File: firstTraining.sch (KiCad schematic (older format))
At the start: 11 parts, among them T1 Transformer_1P_SS, U1 L7805, U2 L78L33_SO8

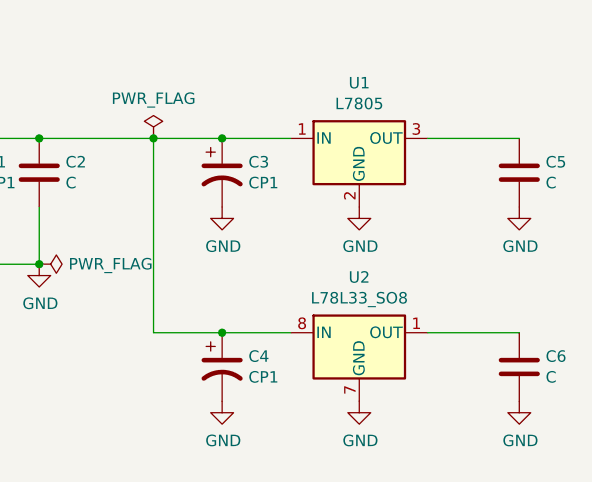
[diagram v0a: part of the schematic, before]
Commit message: GND配線の番号付与追加, 配置実施
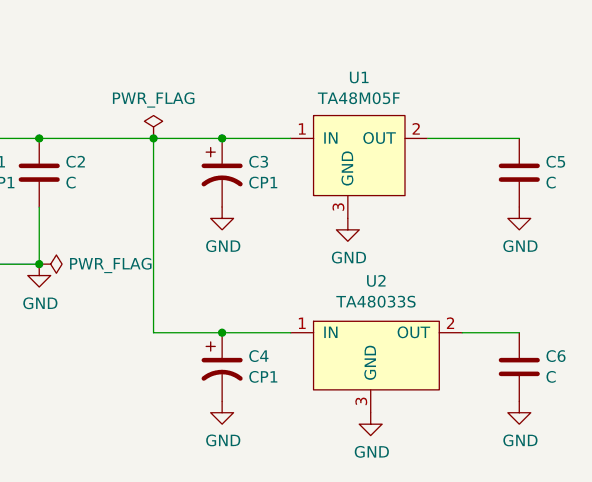
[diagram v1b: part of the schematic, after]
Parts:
- removed U1: L7805, Connector:FanPinHeader_1x03_P2.54mm_Vertical, symbol Regulator_Linear:L7805
- removed U2: L78L33_SO8, Connector:FanPinHeader_1x03_P2.54mm_Vertical, symbol Regulator_Linear:L78L33_SO8
- added U1: TA48M05F, Connector_PinHeader_2.54mm:PinHeader_1x03_P2.54mm_Vertical, symbol newLib:TA48M05F
- added U2: TA48033S, Connector_PinHeader_2.54mm:PinHeader_1x03_P2.54mm_Vertical, symbol newLib:TA48033S
- C2: footprint Capacitor_THT:CP_Radial_D10.0mm_P5.00mm -> Capacitor_THT:C_Disc_D3.0mm_W1.6mm_P2.50mm
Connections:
- net GND: now also U1.3 (GND), U2.3 (GND)
- net at C1.1, C2.1, C3.1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: now also U1.1 (IN), U2.1 (IN)
- net at C5.1: now also U1.2 (OUT)
- net at C6.1: now also U2.2 (OUT)
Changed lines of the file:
@@
 $EndComp
 $Comp
-L power:AC #PWR02
+L power:AC #PWR01
 U 1 1 5BD65D78
 P 2550 1300
-F 0 "#PWR02" H 2550 1200 50  0001 C CNN
+F 0 "#PWR01" H 2550 1200 50  0001 C CNN
 F 1 "AC" H 2550 1575 50  0000 C CNN
 F 2 "" H 2550 1300 50  0001 C CNN
@@
 	1    0    0    -1
 $EndComp
-Wire Wire Line
-	6800 2350 7200 2350
 $Comp
 L power:PWR_FLAG #FLG01
@@
 	2550 1300 2300 1300
 Connection ~ 2550 1300
-Wire Wire Line
-	6800 1500 7200 1500
 $Comp
 L Device:C C5
@@
 $EndComp
 $Comp
-L Regulator_Linear:L7805 U1
-U 1 1 5BD5FA9A
-P 6500 1500
-F 0 "U1" H 6500 1742 50  0000 C CNN
-F 1 "L7805" H 6500 1651 50  0000 C CNN
-F 2 "Connector:FanPinHeader_1x03_P2.54mm_Vertical" H 6525 1350 50  0001 L CIN
-F 3 "http://www.st.com/content/ccc/resource/technical/document/datasheet/41/4f/b3/b0/12/d4/47/88/CD00000444.pdf/files/CD00000444.pdf/jcr:content/translations/en.CD00000444.pdf" H 6500 1450 50  0001 C CNN
-	1    6500 1500
-	1    0    0    -1
-$EndComp
-$Comp
-L Regulator_Linear:L78L33_SO8 U2
-U 1 1 5BD704B9
-P 6500 2350
-F 0 "U2" H 6500 2592 50  0000 C CNN
-F 1 "L78L33_SO8" H 6500 2501 50  0000 C CNN
-F 2 "Connector:FanPinHeader_1x03_P2.54mm_Vertical" H 6600 2550 50  0001 C CIN
-F 3 "http://www.st.com/content/ccc/resource/technical/document/datasheet/15/55/e5/aa/23/5b/43/fd/CD00000446.pdf/files/CD00000446.pdf/jcr:content/translations/en.CD00000446.pdf" H 6700 2350 50  0001 C CNN
-	1    6500 2350
-	1    0    0    -1
-$EndComp
-$Comp
 L Device:Transformer_1P_SS T1
 U 1 1 5BD5E741
@@
 F 0 "C2" H 5215 1696 50  0000 L CNN
 F 1 "C" H 5215 1605 50  0000 L CNN
-F 2 "Capacitor_THT:CP_Radial_D10.0mm_P5.00mm" H 5138 1500 50  0001 C CNN
+F 2 "Capacitor_THT:C_Disc_D3.0mm_W1.6mm_P2.50mm" H 5138 1500 50  0001 C CNN
 F 3 "~" H 5100 1650 50  0001 C CNN
 	1    5100 1650
@@
 	5600 1500 5900 1500
 $Comp
-L power:PWR_FLAG #FLG0101
+L power:PWR_FLAG #FLG04
 U 1 1 5BD8D8CF
 P 5600 1500
-F 0 "#FLG0101" H 5600 1575 50  0001 C CNN
+F 0 "#FLG04" H 5600 1575 50  0001 C CNN
 F 1 "PWR_FLAG" H 5600 1674 50  0000 C CNN
 F 2 "" H 5600 1500 50  0001 C CNN
@@
 	2300 1700 2800 1700
 $Comp
-L power:GND #PWR0101
+L power:GND #PWR03
 U 1 1 5BD927B3
 P 5900 1800
-F 0 "#PWR0101" H 5900 1550 50  0001 C CNN
+F 0 "#PWR03" H 5900 1550 50  0001 C CNN
 F 1 "GND" H 5905 1627 50  0000 C CNN
 F 2 "" H 5900 1800 50  0001 C CNN
@@
 $EndComp
 $Comp
-L power:GND #PWR0102
+L power:GND #PWR05
 U 1 1 5BD927FD
-P 6500 1800
-F 0 "#PWR0102" H 6500 1550 50  0001 C CNN
-F 1 "GND" H 6505 1627 50  0000 C CNN
-F 2 "" H 6500 1800 50  0001 C CNN
-F 3 "" H 6500 1800 50  0001 C CNN
-	1    6500 1800
-	1    0    0    -1
-$EndComp
-$Comp
-L power:GND #PWR0103
+P 6450 1850
+F 0 "#PWR05" H 6450 1600 50  0001 C CNN
+F 1 "GND" H 6455 1677 50  0000 C CNN
+F 2 "" H 6450 1850 50  0001 C CNN
+F 3 "" H 6450 1850 50  0001 C CNN
+	1    6450 1850
+	1    0    0    -1
+$EndComp
+$Comp
+L power:GND #PWR07
 U 1 1 5BD92847
 P 7200 1800
-F 0 "#PWR0103" H 7200 1550 50  0001 C CNN
+F 0 "#PWR07" H 7200 1550 50  0001 C CNN
 F 1 "GND" H 7205 1627 50  0000 C CNN
 F 2 "" H 7200 1800 50  0001 C CNN
@@
 $EndComp
 $Comp
-L power:GND #PWR0104
+L power:GND #PWR08
 U 1 1 5BD92891
 P 7200 2650
-F 0 "#PWR0104" H 7200 2400 50  0001 C CNN
+F 0 "#PWR08" H 7200 2400 50  0001 C CNN
 F 1 "GND" H 7205 2477 50  0000 C CNN
 F 2 "" H 7200 2650 50  0001 C CNN
@@
 $EndComp
 $Comp
-L power:GND #PWR0105
+L power:GND #PWR06
 U 1 1 5BD928DB
-P 6500 2650
-F 0 "#PWR0105" H 6500 2400 50  0001 C CNN
-F 1 "GND" H 6505 2477 50  0000 C CNN
-F 2 "" H 6500 2650 50  0001 C CNN
-F 3 "" H 6500 2650 50  0001 C CNN
-	1    6500 2650
-	1    0    0    -1
-$EndComp
-$Comp
-L power:GND #PWR0106
+P 6550 2700
+F 0 "#PWR06" H 6550 2450 50  0001 C CNN
+F 1 "GND" H 6555 2527 50  0000 C CNN
+F 2 "" H 6550 2700 50  0001 C CNN
+F 3 "" H 6550 2700 50  0001 C CNN
+	1    6550 2700
+	1    0    0    -1
+$EndComp
+$Comp
+L power:GND #PWR04
 U 1 1 5BD92925
 P 5900 2650
-F 0 "#PWR0106" H 5900 2400 50  0001 C CNN
+F 0 "#PWR04" H 5900 2400 50  0001 C CNN
 F 1 "GND" H 5905 2477 50  0000 C CNN
 F 2 "" H 5900 2650 50  0001 C CNN
@@
 $EndComp
 $Comp
-L power:GND #PWR0107
+L power:GND #PWR02
 U 1 1 5BD9296F
 P 5100 2050
-F 0 "#PWR0107" H 5100 1800 50  0001 C CNN
+F 0 "#PWR02" H 5100 1800 50  0001 C CNN
 F 1 "GND" H 5105 1877 50  0000 C CNN
 F 2 "" H 5100 2050 50  0001 C CNN
@@
 Connection ~ 5100 2050
 $Comp
-L power:PWR_FLAG #FLG0102
+L power:PWR_FLAG #FLG03
 U 1 1 5BD929C0
 P 5100 2050
-F 0 "#FLG0102" H 5100 2125 50  0001 C CNN
+F 0 "#FLG03" H 5100 2125 50  0001 C CNN
 F 1 "PWR_FLAG" V 5100 2178 50  0000 L CNN
 F 2 "" H 5100 2050 50  0001 C CNN
@@
 	0    1    1    0
 $EndComp
+$Comp
+L newLib:TA48033S U2
+U 1 1 5BD8C71C
+P 6550 2500
+F 0 "U2" H 6575 2875 50  0000 C CNN
+F 1 "TA48033S" H 6575 2784 50  0000 C CNN
+F 2 "Connector_PinHeader_2.54mm:PinHeader_1x03_P2.54mm_Vertical" H 6550 2500 50  0001 C CNN
+F 3 "" H 6550 2500 50  0001 C CNN
+	1    6550 2500
+	1    0    0    -1
+$EndComp
+Wire Wire Line
+	7200 2350 6950 2350
+$Comp
+L newLib:TA48M05F U1
+U 1 1 5BD8D676
+P 6450 1550
+F 0 "U1" H 6500 1865 50  0000 C CNN
+F 1 "TA48M05F" H 6500 1774 50  0000 C CNN
+F 2 "Connector_PinHeader_2.54mm:PinHeader_1x03_P2.54mm_Vertical" H 6450 1550 50  0001 C CNN
+F 3 "" H 6450 1550 50  0001 C CNN
+	1    6450 1550
+	1    0    0    -1
+$EndComp
+Wire Wire Line
+	7200 1500 6800 1500
 $EndSCHEMATC

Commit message: マウンティングホールを作成
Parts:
- added H1, H2, H3, H4: MountingHole_Pad, symbol Mechanical:MountingHole_Pad
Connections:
- net AC: now also H1.1
- net at T1.2 (AB): now also H2.1
- net at C5.1, U1.2 (OUT): now also H3.1
- net at C6.1, U2.2 (OUT): now also H4.1
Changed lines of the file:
@@
 Wire Wire Line
 	7200 1500 6800 1500
+$Comp
+L Mechanical:MountingHole_Pad H1
+U 1 1 5BD99B15
+P 1700 1200
+F 0 "H1" H 1800 1251 50  0000 L CNN
+F 1 "MountingHole_Pad" H 1800 1160 50  0000 L CNN
+F 2 "" H 1700 1200 50  0001 C CNN
+F 3 "~" H 1700 1200 50  0001 C CNN
+	1    1700 1200
+	1    0    0    -1
+$EndComp
+$Comp
+L Mechanical:MountingHole_Pad H2
+U 1 1 5BD99B7B
+P 1700 1600
+F 0 "H2" H 1800 1651 50  0000 L CNN
+F 1 "MountingHole_Pad" H 1800 1560 50  0000 L CNN
+F 2 "" H 1700 1600 50  0001 C CNN
+F 3 "~" H 1700 1600 50  0001 C CNN
+	1    1700 1600
+	1    0    0    -1
+$EndComp
+Wire Wire Line
+	2300 1300 1700 1300
+Connection ~ 2300 1300
+Wire Wire Line
+	2300 1700 1700 1700
+Connection ~ 2300 1700
+$Comp
+L Mechanical:MountingHole_Pad H3
+U 1 1 5BD9A34D
+P 7900 1400
+F 0 "H3" H 8000 1451 50  0000 L CNN
+F 1 "MountingHole_Pad" H 8000 1360 50  0000 L CNN
+F 2 "" H 7900 1400 50  0001 C CNN
+F 3 "~" H 7900 1400 50  0001 C CNN
+	1    7900 1400
+	1    0    0    -1
+$EndComp
+$Comp
+L Mechanical:MountingHole_Pad H4
+U 1 1 5BD9A3CB
+P 7900 2250
+F 0 "H4" H 8000 2301 50  0000 L CNN
+F 1 "MountingHole_Pad" H 8000 2210 50  0000 L CNN
+F 2 "" H 7900 2250 50  0001 C CNN
+F 3 "~" H 7900 2250 50  0001 C CNN
+	1    7900 2250
+	1    0    0    -1
+$EndComp
+Wire Wire Line
+	7900 1500 7200 1500
+Connection ~ 7200 1500
+Wire Wire Line
+	7900 2350 7200 2350
+Connection ~ 7200 2350
 $EndSCHEMATC

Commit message: スルホとピンヘッダ設定
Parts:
- H1, H2: footprint (none) -> MountingHole:MountingHole_4.5mm_Pad_Via
- H3, H4: footprint (none) -> Connector_PinHeader_2.54mm:PinHeader_1x01_P2.54mm_Horizontal
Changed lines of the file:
@@
 F 0 "H1" H 1800 1251 50  0000 L CNN
 F 1 "MountingHole_Pad" H 1800 1160 50  0000 L CNN
-F 2 "" H 1700 1200 50  0001 C CNN
+F 2 "MountingHole:MountingHole_4.5mm_Pad_Via" H 1700 1200 50  0001 C CNN
 F 3 "~" H 1700 1200 50  0001 C CNN
 	1    1700 1200
@@
 F 0 "H2" H 1800 1651 50  0000 L CNN
 F 1 "MountingHole_Pad" H 1800 1560 50  0000 L CNN
-F 2 "" H 1700 1600 50  0001 C CNN
+F 2 "MountingHole:MountingHole_4.5mm_Pad_Via" H 1700 1600 50  0001 C CNN
 F 3 "~" H 1700 1600 50  0001 C CNN
 	1    1700 1600
@@
 F 0 "H3" H 8000 1451 50  0000 L CNN
 F 1 "MountingHole_Pad" H 8000 1360 50  0000 L CNN
-F 2 "" H 7900 1400 50  0001 C CNN
+F 2 "Connector_PinHeader_2.54mm:PinHeader_1x01_P2.54mm_Horizontal" H 7900 1400 50  0001 C CNN
 F 3 "~" H 7900 1400 50  0001 C CNN
 	1    7900 1400
@@
 F 0 "H4" H 8000 2301 50  0000 L CNN
 F 1 "MountingHole_Pad" H 8000 2210 50  0000 L CNN
-F 2 "" H 7900 2250 50  0001 C CNN
+F 2 "Connector_PinHeader_2.54mm:PinHeader_1x01_P2.54mm_Horizontal" H 7900 2250 50  0001 C CNN
 F 3 "~" H 7900 2250 50  0001 C CNN
 	1    7900 2250

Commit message: GNDパッドに変更
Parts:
- removed D1, D2: DIODE, Diode_THT:D_A-405_P7.62mm_Horizontal, symbol pspice:DIODE
- added D1, D2: D, Diode_THT:D_A-405_P7.62mm_Horizontal, symbol Device:D
- added H5, H6: MountingHole_Pad, Connector_PinHeader_2.54mm:PinHeader_1x01_P2.54mm_Horizontal, symbol Mechanical:MountingHole_Pad
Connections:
- net GND: now also H5.1, H6.1
- net at T1.3 (SA): now also D1.2 (A)
- net at T1.5 (SB): now also D2.2 (A)
- net at C1.1, C2.1, C3.1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: now also D1.1 (K), D2.1 (K)
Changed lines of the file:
@@
 Wire Wire Line
 	4050 1500 4050 2050
-$Comp
-L pspice:DIODE D1
-U 1 1 5BD8A7F3
-P 3800 2300
-F 0 "D1" H 3800 2565 50  0000 C CNN
-F 1 "DIODE" H 3800 2474 50  0000 C CNN
-F 2 "Diode_THT:D_A-405_P7.62mm_Horizontal" H 3800 2300 50  0001 C CNN
-F 3 "~" H 3800 2300 50  0001 C CNN
-	1    3800 2300
-	1    0    0    -1
-$EndComp
-$Comp
-L pspice:DIODE D2
-U 1 1 5BD8A88B
-P 4100 1300
-F 0 "D2" H 4100 1565 50  0000 C CNN
-F 1 "DIODE" H 4100 1474 50  0000 C CNN
-F 2 "Diode_THT:D_A-405_P7.62mm_Horizontal" H 4100 1300 50  0001 C CNN
-F 3 "~" H 4100 1300 50  0001 C CNN
-	1    4100 1300
-	1    0    0    -1
-$EndComp
 Wire Wire Line
 	3900 1300 3600 1300
@@
 	7900 2350 7200 2350
 Connection ~ 7200 2350
+$Comp
+L Device:D D1
+U 1 1 5BD9C8F0
+P 3850 2300
+F 0 "D1" H 3850 2516 50  0000 C CNN
+F 1 "D" H 3850 2425 50  0000 C CNN
+F 2 "Diode_THT:D_A-405_P7.62mm_Horizontal" H 3850 2300 50  0001 C CNN
+F 3 "~" H 3850 2300 50  0001 C CNN
+	1    3850 2300
+	-1   0    0    -1
+$EndComp
+$Comp
+L Device:D D2
+U 1 1 5BD9C97C
+P 4050 1300
+F 0 "D2" H 4050 1516 50  0000 C CNN
+F 1 "D" H 4050 1425 50  0000 C CNN
+F 2 "Diode_THT:D_A-405_P7.62mm_Horizontal" H 4050 1300 50  0001 C CNN
+F 3 "~" H 4050 1300 50  0001 C CNN
+	1    4050 1300
+	-1   0    0    -1
+$EndComp
+Wire Wire Line
+	4300 1300 4200 1300
+Wire Wire Line
+	3700 2300 3600 2300
+$Comp
+L Mechanical:MountingHole_Pad H5
+U 1 1 5BD9E7B6
+P 7900 2950
+F 0 "H5" H 8000 3001 50  0000 L CNN
+F 1 "MountingHole_Pad" H 8000 2910 50  0000 L CNN
+F 2 "Connector_PinHeader_2.54mm:PinHeader_1x01_P2.54mm_Horizontal" H 7900 2950 50  0001 C CNN
+F 3 "~" H 7900 2950 50  0001 C CNN
+	1    7900 2950
+	1    0    0    -1
+$EndComp
+$Comp
+L Mechanical:MountingHole_Pad H6
+U 1 1 5BD9E841
+P 7900 3450
+F 0 "H6" H 8000 3501 50  0000 L CNN
+F 1 "MountingHole_Pad" H 8000 3410 50  0000 L CNN
+F 2 "Connector_PinHeader_2.54mm:PinHeader_1x01_P2.54mm_Horizontal" H 7900 3450 50  0001 C CNN
+F 3 "~" H 7900 3450 50  0001 C CNN
+	1    7900 3450
+	1    0    0    -1
+$EndComp
+$Comp
+L power:GND #PWR09
+U 1 1 5BD9E91C
+P 7900 3050
+F 0 "#PWR09" H 7900 2800 50  0001 C CNN
+F 1 "GND" H 7905 2877 50  0000 C CNN
+F 2 "" H 7900 3050 50  0001 C CNN
+F 3 "" H 7900 3050 50  0001 C CNN
+	1    7900 3050
+	1    0    0    -1
+$EndComp
+$Comp
+L power:GND #PWR010
+U 1 1 5BD9EB43
+P 7900 3550
+F 0 "#PWR010" H 7900 3300 50  0001 C CNN
+F 1 "GND" H 7905 3377 50  0000 C CNN
+F 2 "" H 7900 3550 50  0001 C CNN
+F 3 "" H 7900 3550 50  0001 C CNN
+	1    7900 3550
+	1    0    0    -1
+$EndComp
 $EndSCHEMATC
